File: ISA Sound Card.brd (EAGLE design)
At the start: 163.2 x 108.6 mm, 89 parts, among them IC1 74LS07D, IC10 4051D, IC11 4051D, IC2 74AHC1G07DBV, IC3 74AC14D, IC4 74LVC1G125DBV, IC6 MCP3004, IC8 4051D, IC9 4051D, U1 PCM1808, U10 SN74LVC16T245DGGR, U11 SN74LVC16T245DGGR, U12 SN74LVC16T245DGGR, U3 MIC5365-3.3YD5-TR, U4 PCM5102, U7 MIC5365-3.3YD5-TR, U8 SN74LVC16T245DGGR, X2 LINE_OUT, X3 LINE_IN, X4_ D-SUB-15-SH

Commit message: Updated Eagle symbols for the QMTech CycIV version
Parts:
- removed U$1: QMTECH_5CEFA5F23_SMD, qmtech:QMTECH_5CEFA5F23_SMD
- added CYC_IV_: QMTECH_EP4CE15, qmtech:QMTECH_EP4CE15_SMD
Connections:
- net +3V3: now also CYC_IV_.U7_3, CYC_IV_.U7_4, CYC_IV_.U8_3, CYC_IV_.U8_4; no longer U$1.U5_3, U$1.U5_4, U$1.U6_3, U$1.U6_4
- net +5V: now also CYC_IV_.U7_63, CYC_IV_.U7_64, CYC_IV_.U8_63, CYC_IV_.U8_64; no longer U$1.U5_63, U$1.U5_64, U$1.U6_63, U$1.U6_64
- net ADC_DOUT: now also CYC_IV_.U7_57; no longer U$1.U6_57
- net CONF_DONE: now also CYC_IV_.JP3_5; no longer U$1.2
- net DAC_DIN: now also CYC_IV_.U7_60; no longer U$1.U6_60
- net DRQ_HI_SEL_A0: now also CYC_IV_.U8_16; no longer U$1.U5_16
- net DRQ_HI_SEL_A1: now also CYC_IV_.U8_17; no longer U$1.U5_17
- net DRQ_HI_SEL_A2: now also CYC_IV_.U8_18; no longer U$1.U5_18
- net DRQ_HI_TRIG_N: now also CYC_IV_.U8_15; no longer U$1.U5_15
- net DRQ_LO_SEL_A0: now also CYC_IV_.U7_16; no longer U$1.U6_16
- net DRQ_LO_SEL_A1: now also CYC_IV_.U7_17; no longer U$1.U6_17
- net DRQ_LO_SEL_A2: now also CYC_IV_.U7_18; no longer U$1.U6_18
- net DRQ_LO_TRIG_N: now also CYC_IV_.U7_15; no longer U$1.U6_15
- net FPGA_0WS: now also CYC_IV_.U8_40; no longer U$1.U5_40
- net FPGA_ADS0: now also CYC_IV_.JP3_1; no longer U$1.5
- net FPGA_AEN: now also CYC_IV_.U8_45; no longer U$1.U5_45
- net FPGA_BALE: now also CYC_IV_.U8_22; no longer U$1.U5_22
- net FPGA_CLK: now also CYC_IV_.U7_25; no longer U$1.U6_25
- net FPGA_DACK0_N: now also CYC_IV_.U8_21; no longer U$1.U5_21
- net FPGA_DACK1_N: now also CYC_IV_.U7_26; no longer U$1.U6_26
- net FPGA_DACK2_N: now also CYC_IV_.U8_23; no longer U$1.U5_23
- net FPGA_DACK3_N: now also CYC_IV_.U8_25; no longer U$1.U5_25
- net FPGA_DACK5_N: now also CYC_IV_.U7_22; no longer U$1.U6_22
- net FPGA_DACK6_N: now also CYC_IV_.U8_19; no longer U$1.U5_19
- net FPGA_DACK7_N: now also CYC_IV_.U7_21; no longer U$1.U6_21
- net FPGA_DCLK: now also CYC_IV_.JP3_2; no longer U$1.1
- net FPGA_IOCHK: now also CYC_IV_.U8_50; no longer U$1.U5_50
- net FPGA_IOCHRDY: now also CYC_IV_.U8_60; no longer U$1.U5_60
- net FPGA_IOCS16_N: now also CYC_IV_.U8_56; no longer U$1.U5_56
- net FPGA_IOR_N: now also CYC_IV_.U7_27; no longer U$1.U6_27
- net FPGA_IOW_N: now also CYC_IV_.U8_26; no longer U$1.U5_26
- net FPGA_JOY_B1: now also CYC_IV_.U7_50; no longer U$1.U6_50
- net FPGA_JOY_B2: now also CYC_IV_.U7_51; no longer U$1.U6_51
- net FPGA_JOY_B3: now also CYC_IV_.U7_52; no longer U$1.U6_52
- net FPGA_JOY_B4: now also CYC_IV_.U7_53; no longer U$1.U6_53
- net FPGA_LA17: now also CYC_IV_.U7_11; no longer U$1.U6_11
- net FPGA_LA18: now also CYC_IV_.U8_11; no longer U$1.U5_11
- net FPGA_LA19: now also CYC_IV_.U7_12; no longer U$1.U6_12
- net FPGA_LA20: now also CYC_IV_.U8_12; no longer U$1.U5_12
- net FPGA_LA21: now also CYC_IV_.U7_13; no longer U$1.U6_13
- net FPGA_LA22: now also CYC_IV_.U8_13; no longer U$1.U5_13
- net FPGA_LA23: now also CYC_IV_.U7_14; no longer U$1.U6_14
- net FPGA_LA_DIR: now also CYC_IV_.U8_20; no longer U$1.U5_20
- net FPGA_MASTER_N: now also CYC_IV_.U8_58; no longer U$1.U5_58
- net FPGA_MEMCS16_N: now also CYC_IV_.U8_54; no longer U$1.U5_54
- net FPGA_MEMR_N: now also CYC_IV_.U8_28; no longer U$1.U5_28
- net FPGA_MEMW_N: now also CYC_IV_.U8_27; no longer U$1.U5_27
- net FPGA_MIDI_RXD: now also CYC_IV_.U7_54; no longer U$1.U6_54
- net FPGA_MIDI_TXD: now also CYC_IV_.U7_56; no longer U$1.U6_56
- net FPGA_OSC: now also CYC_IV_.U7_23; no longer U$1.U6_23
- net FPGA_REFRESH_N: now also CYC_IV_.U8_52; no longer U$1.U5_52
- net FPGA_RES_DRV: now also CYC_IV_.U7_43; no longer U$1.U6_43
- net FPGA_SA0: now also CYC_IV_.U7_29; no longer U$1.U6_29
- net FPGA_SA1: now also CYC_IV_.U8_29; no longer U$1.U5_29
- net FPGA_SA10: now also CYC_IV_.U7_34; no longer U$1.U6_34
- net FPGA_SA11: now also CYC_IV_.U8_34; no longer U$1.U5_34
- net FPGA_SA12: now also CYC_IV_.U7_35; no longer U$1.U6_35
- net FPGA_SA13: now also CYC_IV_.U8_35; no longer U$1.U5_35
- net FPGA_SA14: now also CYC_IV_.U7_36; no longer U$1.U6_36
- net FPGA_SA15: now also CYC_IV_.U8_36; no longer U$1.U5_36
- net FPGA_SA159_DIR: now also CYC_IV_.U7_41; no longer U$1.U6_41
- net FPGA_SA16: now also CYC_IV_.U8_43; no longer U$1.U5_43
- net FPGA_SA17: now also CYC_IV_.U7_44; no longer U$1.U6_44
- net FPGA_SA18: now also CYC_IV_.U8_44; no longer U$1.U5_44
- net FPGA_SA19: now also CYC_IV_.U7_45; no longer U$1.U6_45
- net FPGA_SA2: now also CYC_IV_.U7_30; no longer U$1.U6_30
- net FPGA_SA3: now also CYC_IV_.U8_30; no longer U$1.U5_30
- net FPGA_SA4: now also CYC_IV_.U7_31; no longer U$1.U6_31
- net FPGA_SA5: now also CYC_IV_.U8_31; no longer U$1.U5_31
- net FPGA_SA6: now also CYC_IV_.U7_32; no longer U$1.U6_32
- net FPGA_SA7: now also CYC_IV_.U8_32; no longer U$1.U5_32
- net FPGA_SA8: now also CYC_IV_.U7_33; no longer U$1.U6_33
- net FPGA_SA9: now also CYC_IV_.U8_33; no longer U$1.U5_33
- net FPGA_SBHE: now also CYC_IV_.U8_14; no longer U$1.U5_14
- net FPGA_SD0: now also CYC_IV_.U7_46; no longer U$1.U6_46
- net FPGA_SD1: now also CYC_IV_.U8_46; no longer U$1.U5_46
- net FPGA_SD10: now also CYC_IV_.U8_9; no longer U$1.U5_9
- net FPGA_SD11: now also CYC_IV_.U7_9; no longer U$1.U6_9
- net FPGA_SD12: now also CYC_IV_.U8_8; no longer U$1.U5_8
- net FPGA_SD13: now also CYC_IV_.U7_8; no longer U$1.U6_8
- net FPGA_SD14: now also CYC_IV_.U8_7; no longer U$1.U5_7
- net FPGA_SD15: now also CYC_IV_.U7_7; no longer U$1.U6_7
- net FPGA_SD159_DIR: now also CYC_IV_.U8_24; no longer U$1.U5_24
- net FPGA_SD2: now also CYC_IV_.U7_47; no longer U$1.U6_47
- net FPGA_SD3: now also CYC_IV_.U8_47; no longer U$1.U5_47
- net FPGA_SD4: now also CYC_IV_.U7_48; no longer U$1.U6_48
- net FPGA_SD5: now also CYC_IV_.U8_48; no longer U$1.U5_48
- net FPGA_SD6: now also CYC_IV_.U7_49; no longer U$1.U6_49
- net FPGA_SD7: now also CYC_IV_.U8_49; no longer U$1.U5_49
- net FPGA_SD70_DIR: now also CYC_IV_.U8_59; no longer U$1.U5_59
- net FPGA_SD8: now also CYC_IV_.U8_10; no longer U$1.U5_10
- net FPGA_SD9: now also CYC_IV_.U7_10; no longer U$1.U6_10
- net FPGA_SMEMR_N: now also CYC_IV_.U7_42; no longer U$1.U6_42
- net FPGA_SMEMW_N: now also CYC_IV_.U8_42; no longer U$1.U5_42
- net FPGA_TC: now also CYC_IV_.U7_24; no longer U$1.U6_24
- net GND: now also CYC_IV_.JP3_6, CYC_IV_.U7_1, CYC_IV_.U7_2, CYC_IV_.U7_5, CYC_IV_.U7_6, CYC_IV_.U7_61, CYC_IV_.U7_62, CYC_IV_.U8_1, CYC_IV_.U8_2, CYC_IV_.U8_5, CYC_IV_.U8_6, CYC_IV_.U8_61, CYC_IV_.U8_62; no longer U$1.6, U$1.U5_1, U$1.U5_2, U$1.U5_5, U$1.U5_6, U$1.U5_61, U$1.U5_62, U$1.U6_1, U$1.U6_2, U$1.U6_5, U$1.U6_6, U$1.U6_61, U$1.U6_62
- net I2S_BCK: now also CYC_IV_.U7_58; no longer U$1.U6_58
- net I2S_LRCK: now also CYC_IV_.U7_59; no longer U$1.U6_59
- net I2S_SCK: now also CYC_IV_.U7_55; no longer U$1.U6_55
- net IRQ_HI_SEL_A0: now also CYC_IV_.U8_38; no longer U$1.U5_38
- net IRQ_HI_SEL_A1: now also CYC_IV_.U8_39; no longer U$1.U5_39
- net IRQ_HI_SEL_A2: now also CYC_IV_.U8_41; no longer U$1.U5_41
- net IRQ_HI_TRIG_N: now also CYC_IV_.U8_37; no longer U$1.U5_37
- net IRQ_LO_SEL_A0: now also CYC_IV_.U7_37; no longer U$1.U6_37
- net IRQ_LO_SEL_A1: now also CYC_IV_.U7_40; no longer U$1.U6_40
- net IRQ_LO_SEL_A2: now also CYC_IV_.U7_39; no longer U$1.U6_39
- net IRQ_LO_TRIG_N: now also CYC_IV_.U7_38; no longer U$1.U6_38
- net JOY_CLK: now also CYC_IV_.U8_57; no longer U$1.U5_57
- net JOY_CS_N: now also CYC_IV_.U8_51; no longer U$1.U5_51
- net JOY_DIN: now also CYC_IV_.U8_53; no longer U$1.U5_53
- net JOY_DOUT: now also CYC_IV_.U8_55; no longer U$1.U5_55
- net N$8: now also CYC_IV_.U7_20; no longer U$1.U6_20
- net N$9: now also CYC_IV_.U7_28; no longer U$1.U6_28
- net NCONFIG: now also CYC_IV_.JP3_3; no longer U$1.3
- net NSTATUS: now also CYC_IV_.JP3_4; no longer U$1.4
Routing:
- net GND: track 119.8 -> 121.9 mm, vias 73 -> 76
- net +3V3: track 396.2 -> 394.6 mm
- net +5V: vias 28 -> 27

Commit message: Add Quartus project
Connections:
- net FPGA_0WS renamed FPGA_ZERO_WAIT
- net FPGA_SA159_DIR renamed FPGA_SA158_DIR
- net FPGA_SD159_DIR renamed FPGA_SD158_DIR
- removed net N$77: C60.1, U4.3
- new net CLK14_6N: CYC_IV_.U8_6
- new net CLK15_6P: CYC_IV_.U8_5
- net ADC_3V3_FILT: no longer U1.11
- net GND: now also C60.1, U1.11, U4.12, U4.3; no longer CYC_IV_.U8_5, CYC_IV_.U8_6
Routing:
- net N$77: track 8.62 -> 0.00 mm, vias 2 -> 0
- net GND: track 121.9 -> 125.7 mm, vias 76 -> 78
- net ADC_3V3_FILT: track 16.0 -> 17.9 mm, vias 0 -> 2

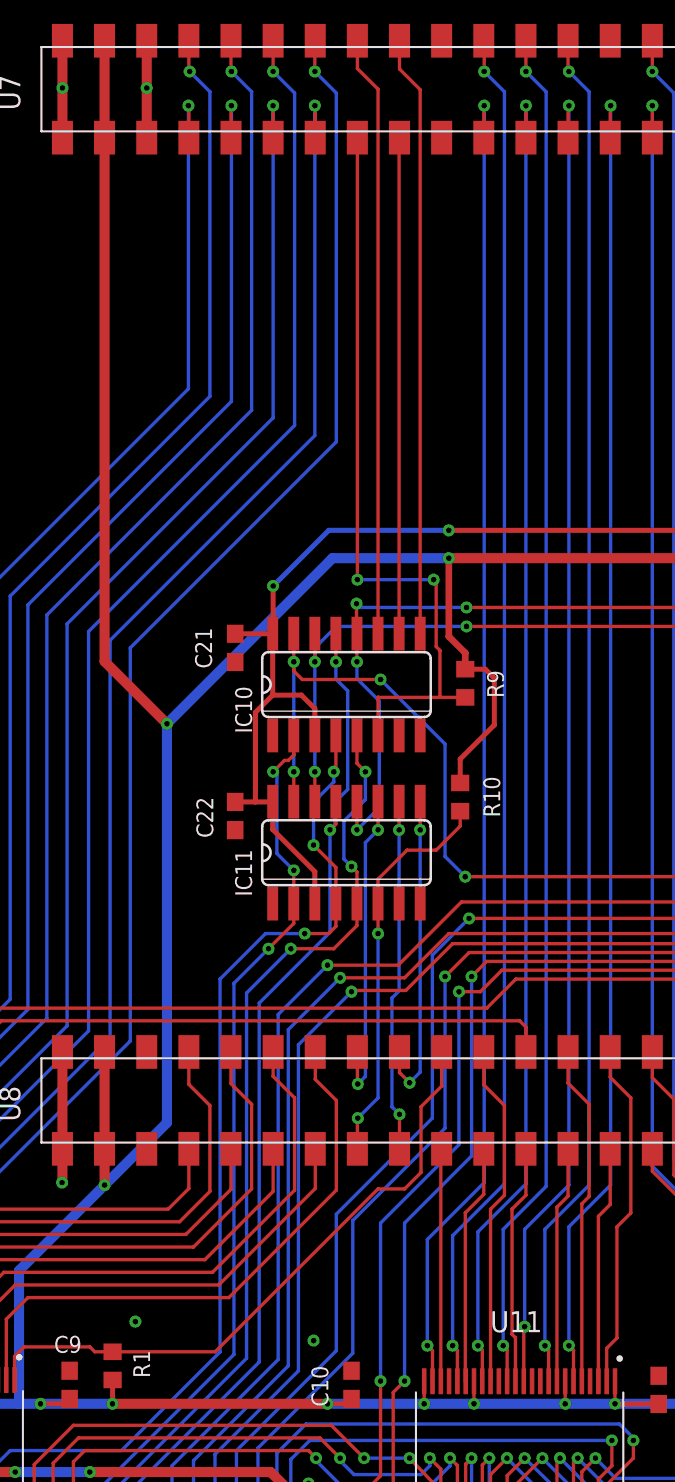
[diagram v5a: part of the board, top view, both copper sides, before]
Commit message: Hooked up ISA CLK and OSC to the FPGA Clk-in pins
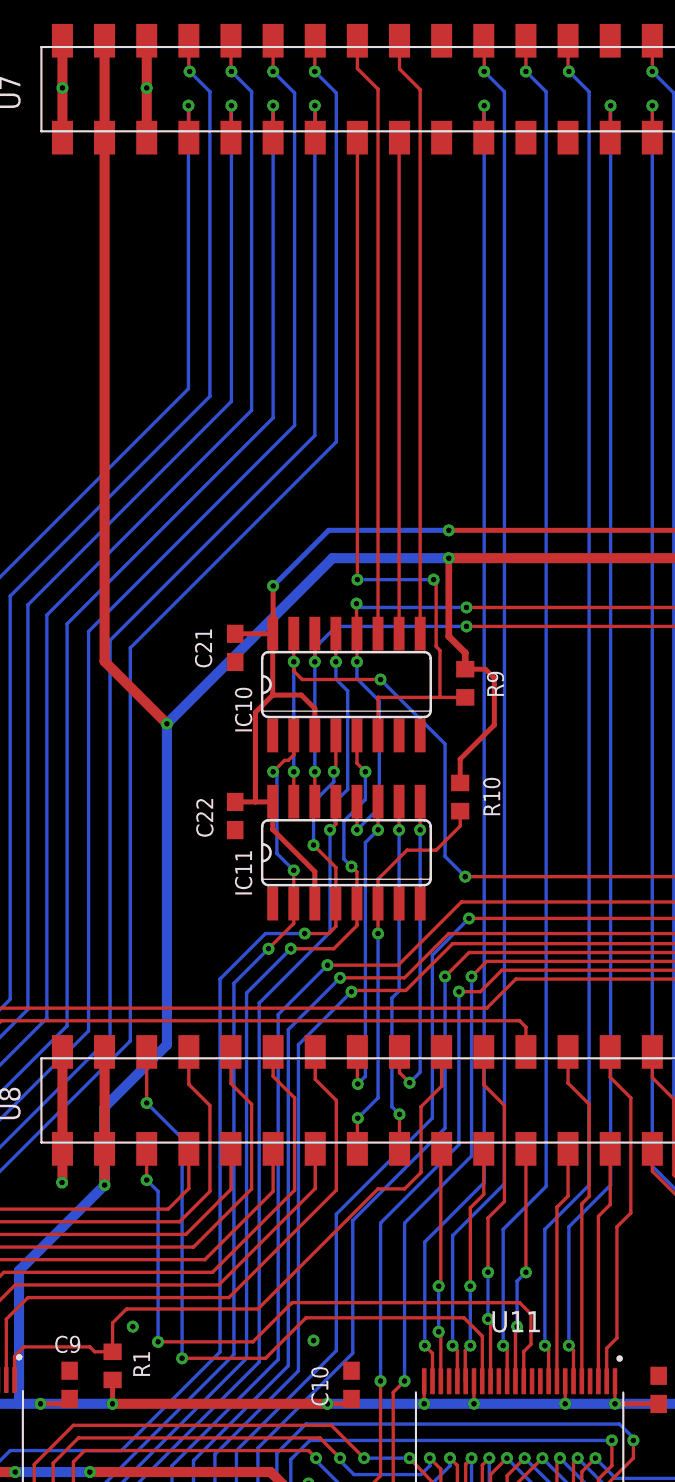
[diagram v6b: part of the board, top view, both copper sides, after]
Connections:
- net N$13 renamed 5V_TO_FUSE
- removed net CLK14_6N: CYC_IV_.U8_6
- removed net CLK15_6P: CYC_IV_.U8_5
- net FPGA_CLK: now also CYC_IV_.U8_5; no longer CYC_IV_.U7_25
- net FPGA_OSC: now also CYC_IV_.U8_6; no longer CYC_IV_.U7_23
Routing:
- net FPGA_CLK: track 80.0 -> 39.9 mm
- net FPGA_OSC: track 80.1 -> 41.6 mm
- net FPGA_LA_DIR: track 38.5 -> 39.6 mm
- net FPGA_DACK2_N: track 14.4 -> 14.3 mm, vias 0 -> 2
- net FPGA_BALE: track 20.7 -> 20.8 mm, vias 0 -> 2
- net FPGA_DACK6_N: track 14.0 -> 14.1 mm, vias 0 -> 2
- net FPGA_DACK0_N: vias 0 -> 2

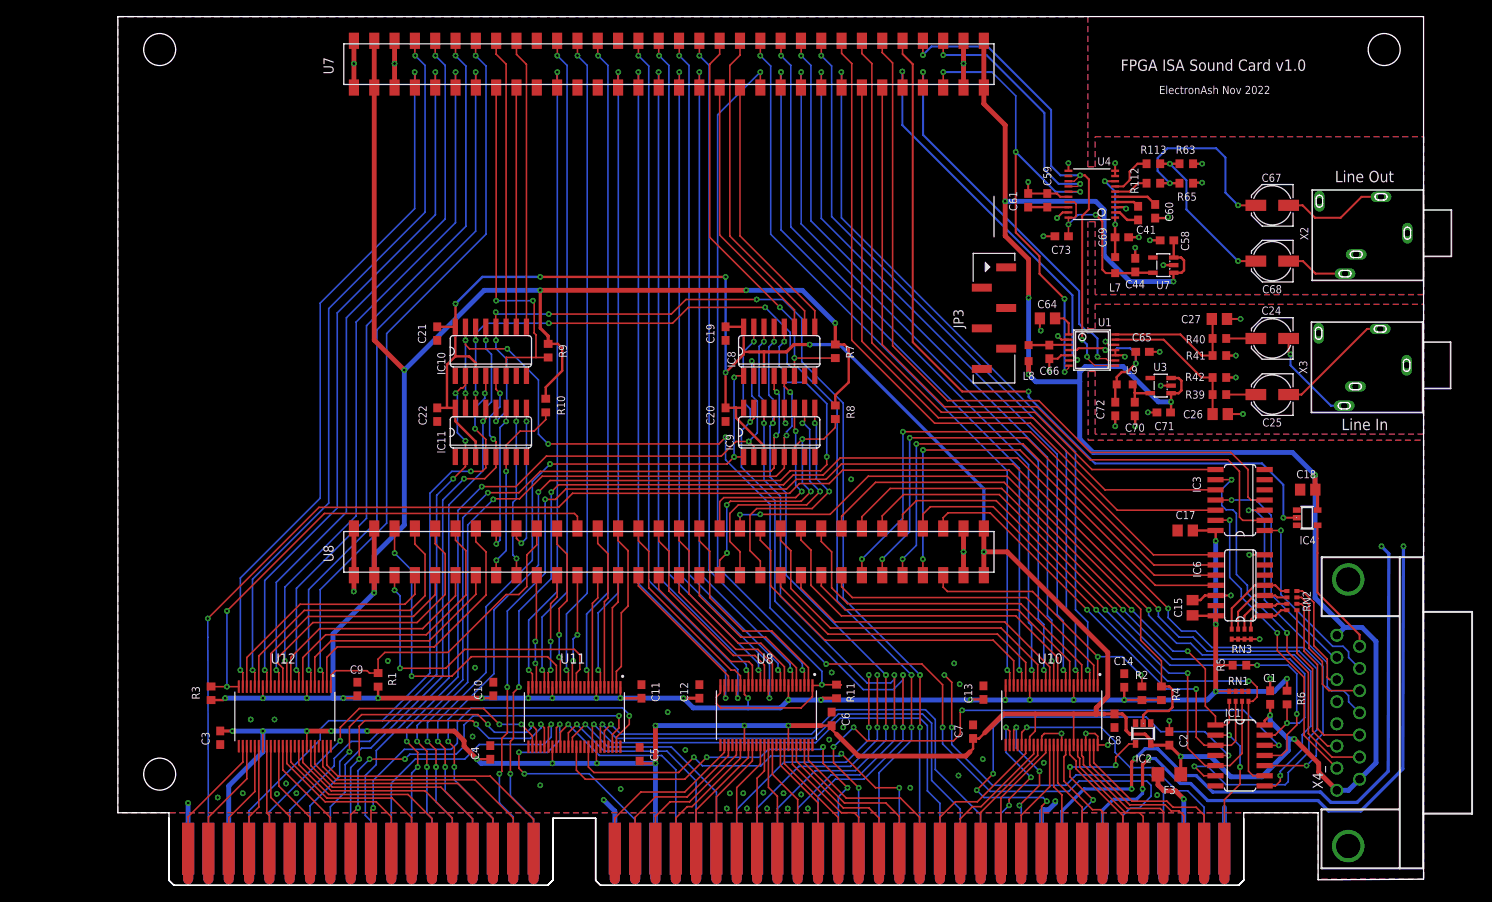
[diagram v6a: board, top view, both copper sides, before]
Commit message: Changed joystick port DB15 for the correct (female) connector
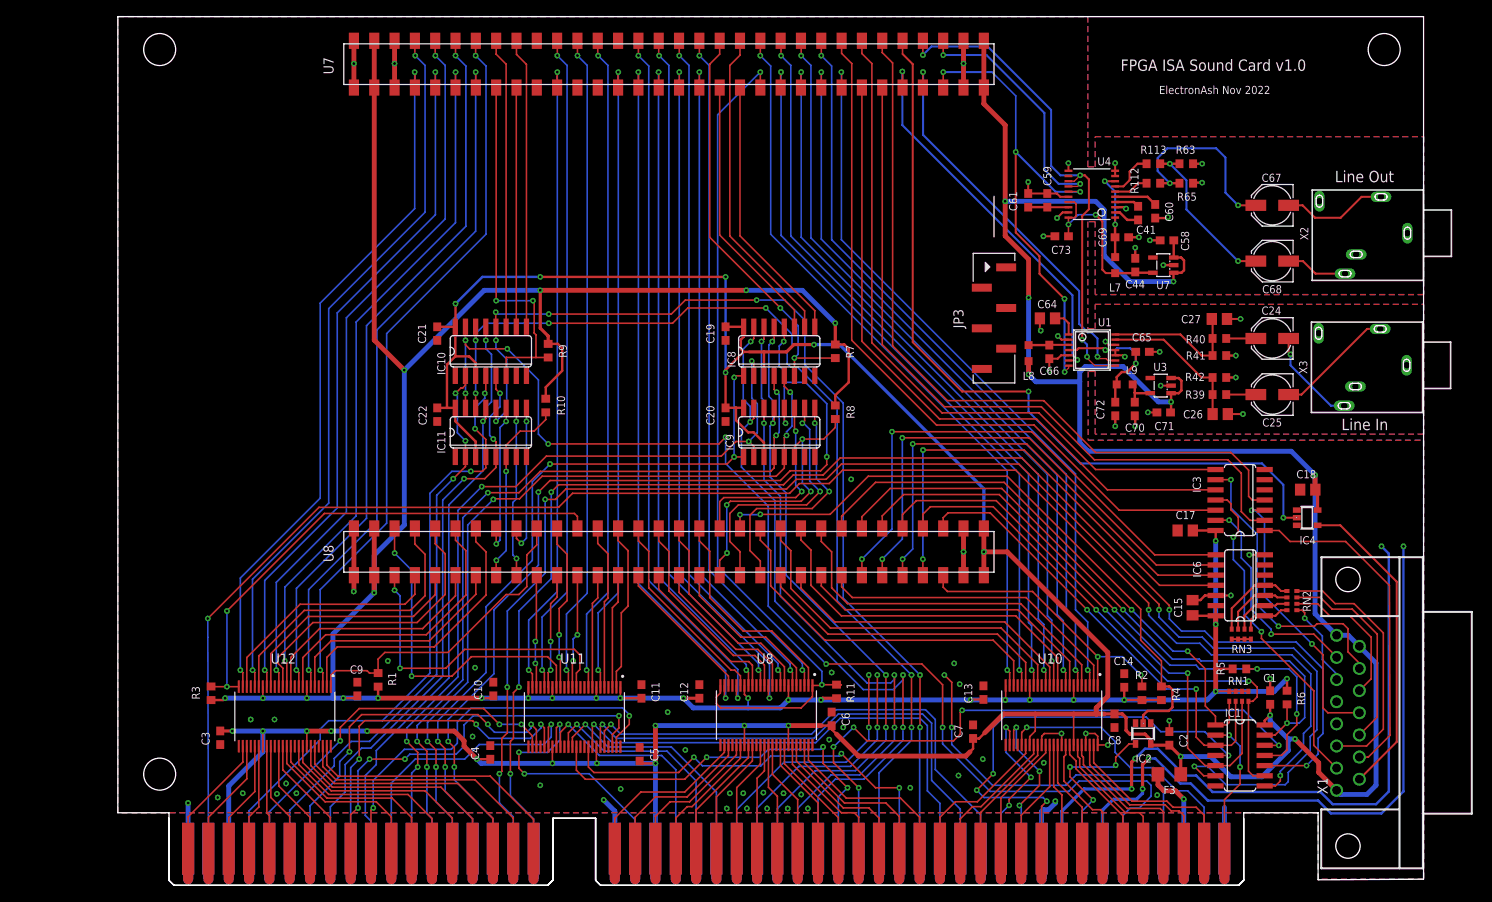
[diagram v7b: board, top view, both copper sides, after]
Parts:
- removed X4_: D-SUB-15-SH, con-thomas-betts:H5M15RA
- added X1: D-SUB15-H5R15RA, con-thomas-betts:H5R15RA
- moved R5 0.46 mm to (160.8, 35.4)
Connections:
- net +5V: now also X1.1, X1.8, X1.9; no longer X4_.1, X4_.8, X4_.9
- net GND: now also X1.4, X1.5; no longer X4_.4, X4_.5
- net JOY_B1_N: now also X1.2; no longer X4_.2
- net JOY_B2_N: now also X1.7; no longer X4_.7
- net JOY_B3_N: now also X1.10; no longer X4_.10
- net JOY_B4_N: now also X1.14; no longer X4_.14
- net JOY_X1: now also X1.3; no longer X4_.3
- net JOY_X2: now also X1.11; no longer X4_.11
- net JOY_Y1: now also X1.6; no longer X4_.6
- net JOY_Y2: now also X1.13; no longer X4_.13
- net MIDI_RXD: now also X1.12; no longer X4_.12
- net MIDI_TXD: now also X1.15; no longer X4_.15
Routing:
- net MIDI_TXD: track 17.3 -> 39.4 mm
- net JOY_B4_N: track 24.1 -> 42.1 mm, vias 1 -> 0
- net JOY_Y1: track 14.1 -> 31.7 mm
- net JOY_B2_N: track 29.1 -> 41.2 mm, vias 1 -> 2
- net JOY_B1_N: track 38.3 -> 27.6 mm
- net JOY_B3_N: track 46.8 -> 37.3 mm
- net JOY_X1: track 19.7 -> 11.1 mm, vias 0 -> 1
- net JOY_Y2: track 17.5 -> 25.5 mm
- net JOY_X2: track 22.6 -> 18.3 mm
- net N$14: track 79.8 -> 81.8 mm
- net N$27: track 83.6 -> 85.3 mm
- net +5V: track 607.8 -> 609.1 mm
- net GND: track 125.7 -> 124.6 mm, vias 78 -> 77
- net FPGA_MIDI_TXD: track 98.1 -> 99.2 mm
- net JOY_CS_N: track 65.5 -> 66.3 mm
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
